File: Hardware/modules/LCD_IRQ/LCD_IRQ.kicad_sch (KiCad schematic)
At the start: 18 parts, among them J1 Bus_PCI_6502, U1 74HC138, U2 W65C22SxP

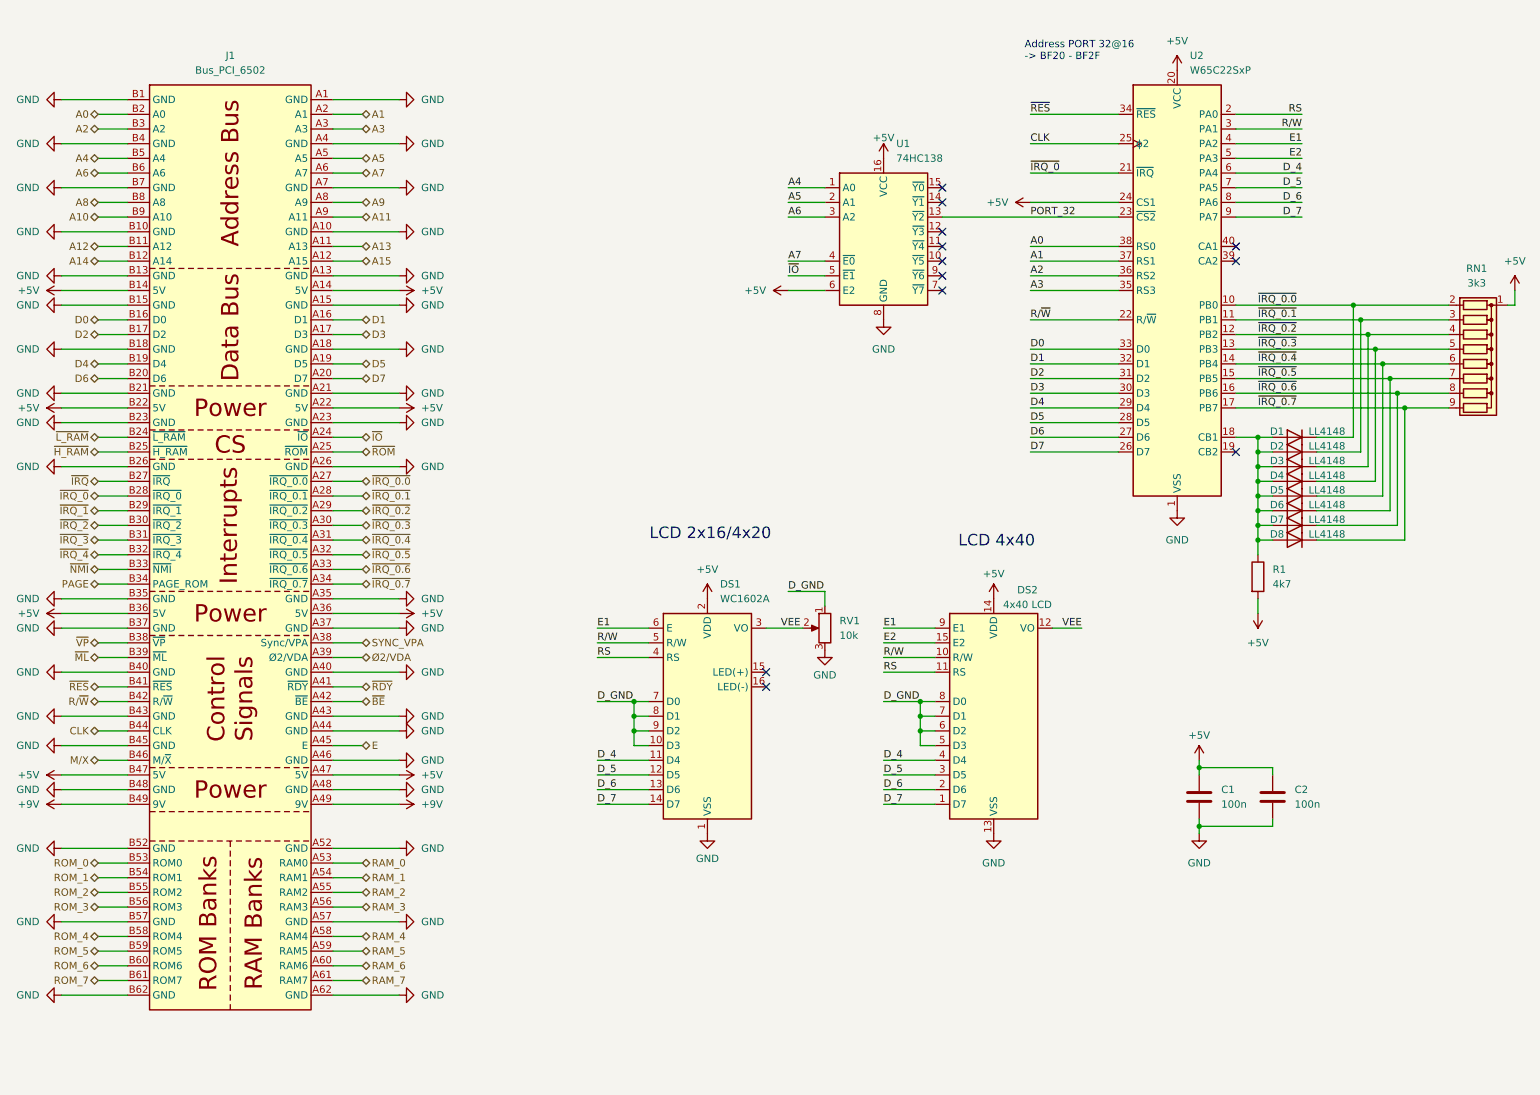
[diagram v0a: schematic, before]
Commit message: Hardware Update Add MyCPU VGA Module Beautify all Schematics minor Error corrections Readme Update
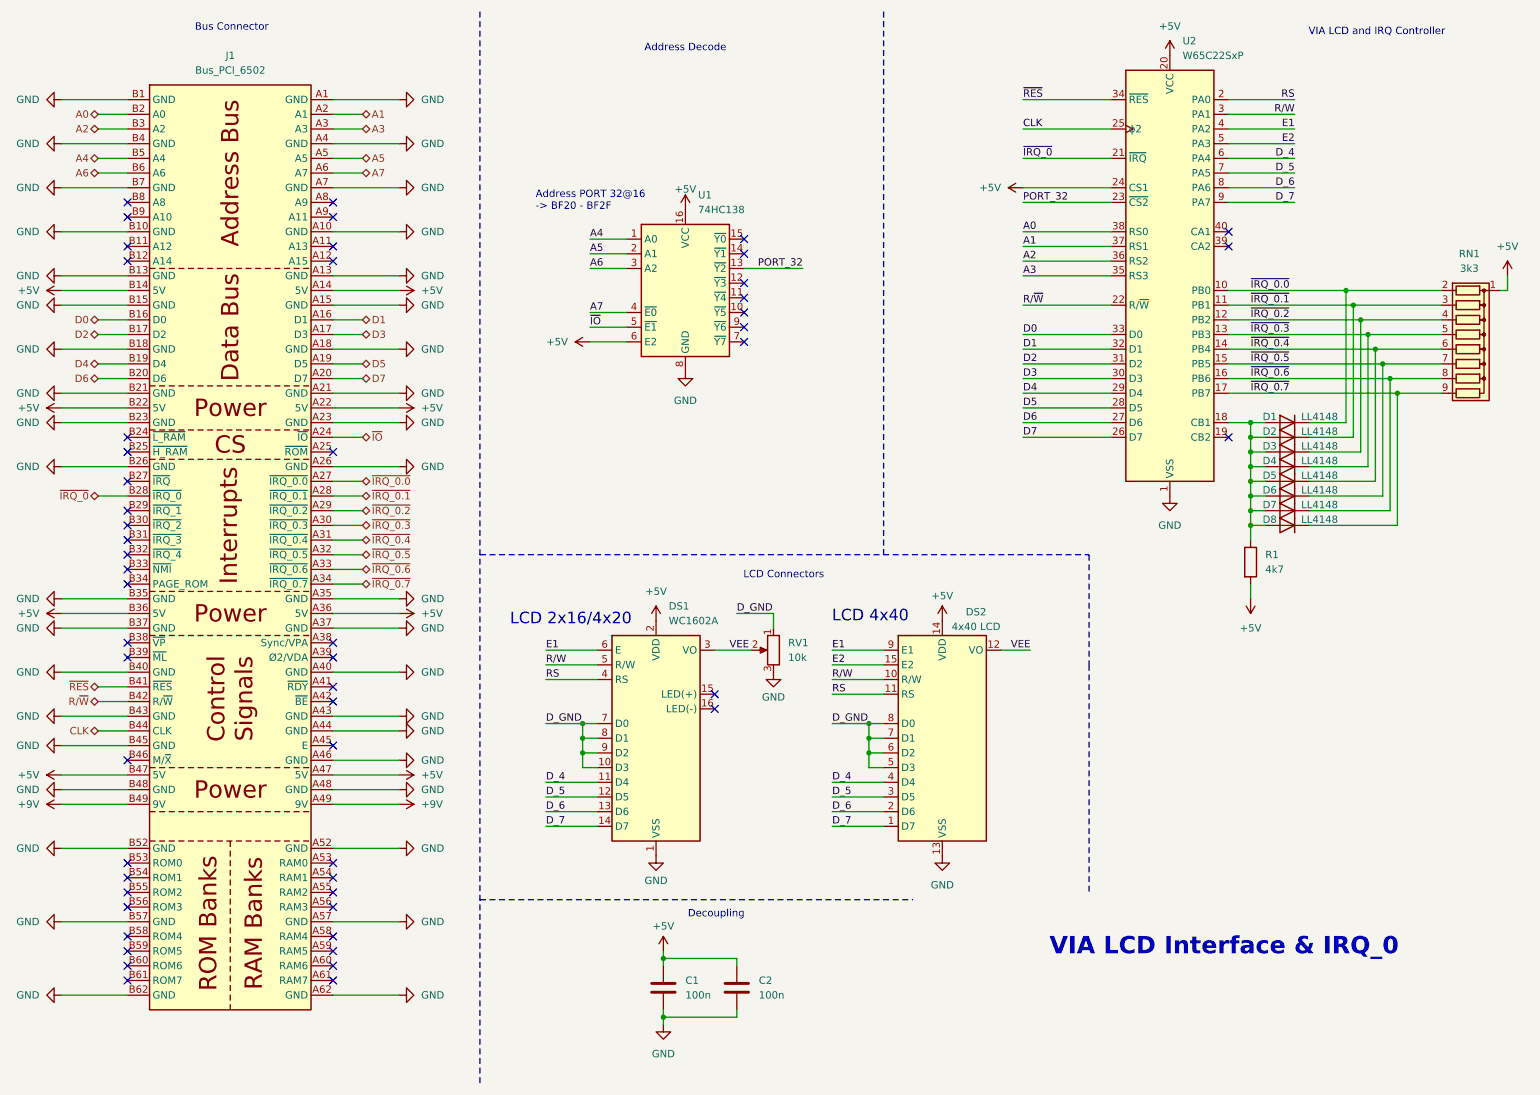
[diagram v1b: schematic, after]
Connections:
- net A10: no longer names the net of J1.B9 (A10)
- net A11: no longer names the net of J1.A9 (A11)
- net A12: no longer names the net of J1.B11 (A12)
- net A13: no longer names the net of J1.A11 (A13)
- net A14: no longer names the net of J1.B12 (A14)
- net A15: no longer names the net of J1.A12 (A15)
- net A8: no longer names the net of J1.B8 (A8)
- net A9: no longer names the net of J1.A8 (A9)
- net E: no longer names the net of J1.A45 (E)
- net M/X: no longer names the net of J1.B46 (M/~{X})
- net PAGE: no longer names the net of J1.B34 (PAGE_ROM)
- net RAM_0: no longer names the net of J1.A53 (RAM0)
- net RAM_1: no longer names the net of J1.A54 (RAM1)
- net RAM_2: no longer names the net of J1.A55 (RAM2)
- net RAM_3: no longer names the net of J1.A56 (RAM3)
- net RAM_4: no longer names the net of J1.A58 (RAM4)
- net RAM_5: no longer names the net of J1.A59 (RAM5)
- net RAM_6: no longer names the net of J1.A60 (RAM6)
- net RAM_7: no longer names the net of J1.A61 (RAM7)
- net ROM_0: no longer names the net of J1.B53 (ROM0)
- net ROM_1: no longer names the net of J1.B54 (ROM1)
- net ROM_2: no longer names the net of J1.B55 (ROM2)
- net ROM_3: no longer names the net of J1.B56 (ROM3)
- net ROM_4: no longer names the net of J1.B58 (ROM4)
- net ROM_5: no longer names the net of J1.B59 (ROM5)
- net ROM_6: no longer names the net of J1.B60 (ROM6)
- net ROM_7: no longer names the net of J1.B61 (ROM7)
- net SYNC_VPA: no longer names the net of J1.A38 (Sync/VPA)
- net ~{BE}: no longer names the net of J1.A42 (~{BE})
- net ~{H_RAM}: no longer names the net of J1.B25 (~{H_RAM})
- net ~{IRQ_1}: no longer names the net of J1.B29 (~{IRQ_1})
- net ~{IRQ_2}: no longer names the net of J1.B30 (~{IRQ_2})
- net ~{IRQ_3}: no longer names the net of J1.B31 (~{IRQ_3})
- net ~{IRQ_4}: no longer names the net of J1.B32 (~{IRQ_4})
- net ~{IRQ}: no longer names the net of J1.B27 (~{IRQ})
- net ~{L_RAM}: no longer names the net of J1.B24 (~{L_RAM})
- net ~{ML}: no longer names the net of J1.B39 (~{ML})
- net ~{NMI}: no longer names the net of J1.B33 (~{NMI})
- net ~{RDY}: no longer names the net of J1.A41 (~{RDY})
- net ~{ROM}: no longer names the net of J1.A25 (~{ROM})
- net ~{VP}: no longer names the net of J1.B38 (~{VP})
- net Ø2/VDA: no longer names the net of J1.A39 (Ø2/VDA)
- no-connect marks 12 -> 54
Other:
- note added: "Address Decode"
- note added: "Bus Connector"
- note added: "Decoupling"
- note added: "LCD Connectors"
- note added: "VIA LCD Interface & IRQ_0"
- note added: "VIA LCD and IRQ Controller"
- company: (none) -> Synthron
- title: (none) -> S65xx Computer System
- moved on the sheet: C1, C2, D1, D2, D3, D4, D5, D6, D7, D8, DS1, DS2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

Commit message: Hardware Review Pt. 1 fix Address Decoding for Strobe Generators add bulk capacitance to every board fix wiring of Prototyping Board
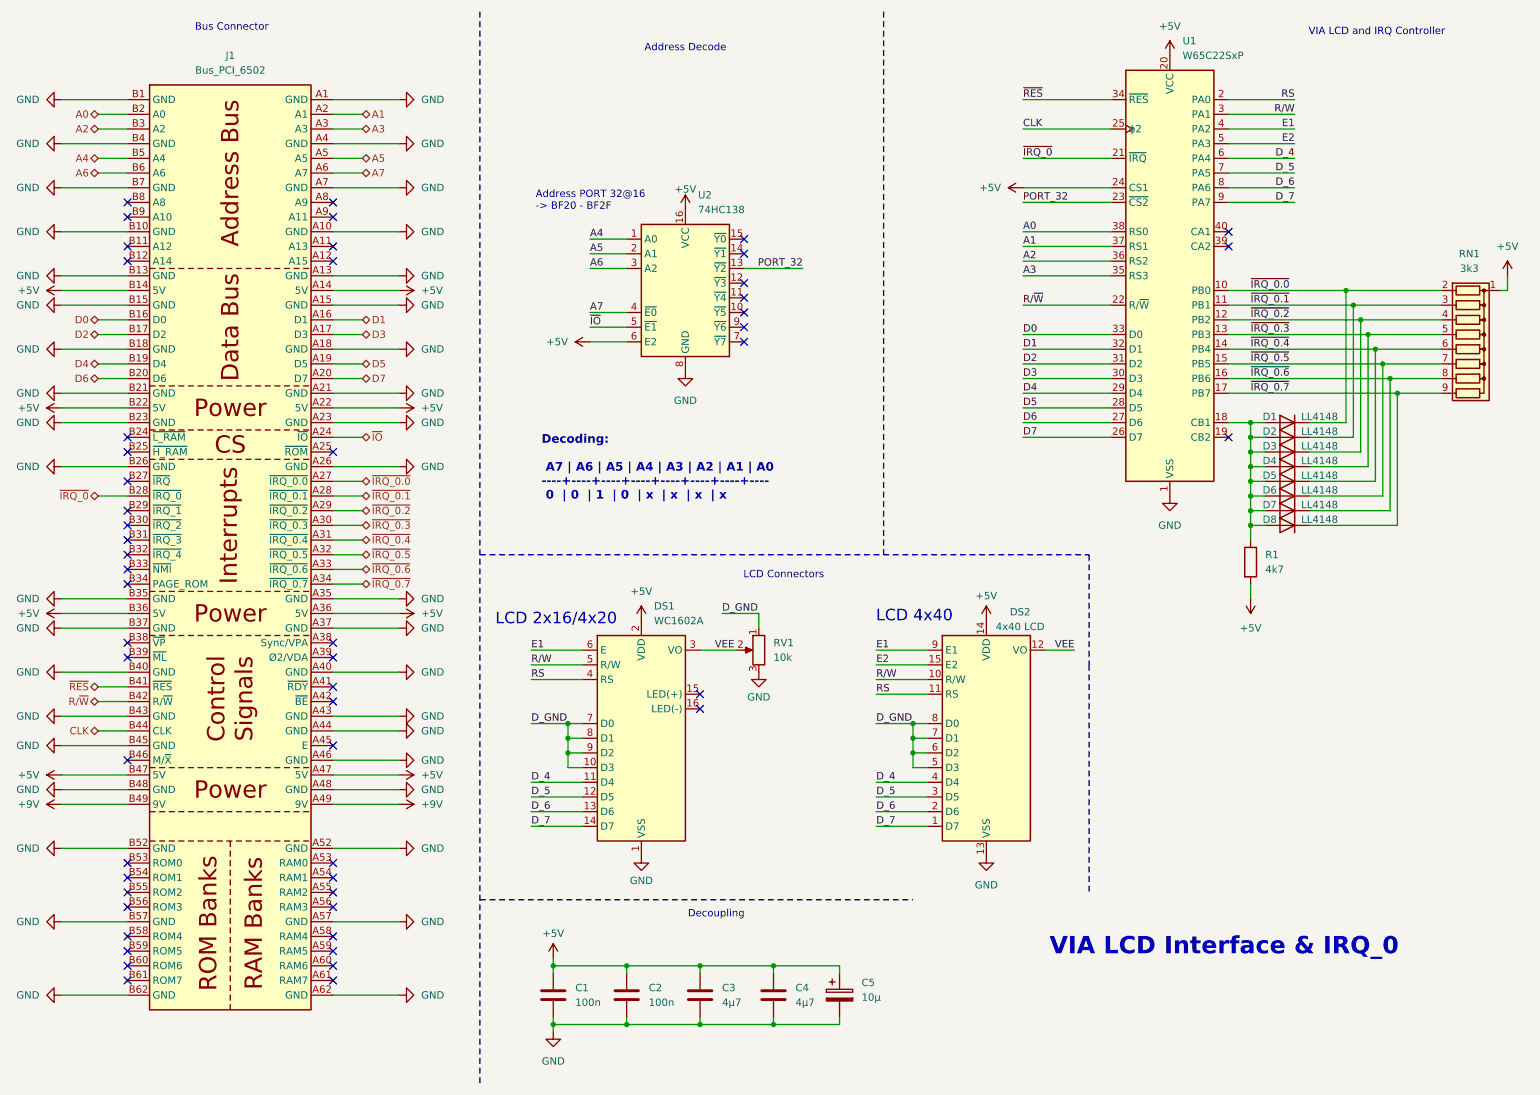
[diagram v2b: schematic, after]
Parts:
- added C3, C4: 4µ7, Capacitor_SMD:C_0805_2012Metric, symbol Device:C
- added C5: 10µ, Capacitor_THT:CP_Radial_D5.0mm_P2.50mm, symbol Device:C_Polarized
- renumbered U2 to U1, U1 to U2
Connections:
- net +5V: now also C3.1, C4.1, C5.1
- net GND: now also C3.2, C4.2, C5.2
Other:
- note added: "Decoding: A7 | A6 | A5 | A4 | A3 | A2 | A1 | A0 ----+----+----+----+----+----+----+---- 0 | 0 | 1 | 0 | x | x | x | x"
- moved on the sheet: C1, C2, DS1, DS2, RV1
